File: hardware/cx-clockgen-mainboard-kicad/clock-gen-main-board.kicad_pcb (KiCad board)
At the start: 2 copper layers, 70 x 64.4 mm, 17 parts, among them J1 Conn_01x03_Pin, J2 Conn_01x03_Pin, J3 Headswitch_SMA, J8 Conn_Coaxial, U1 Pico

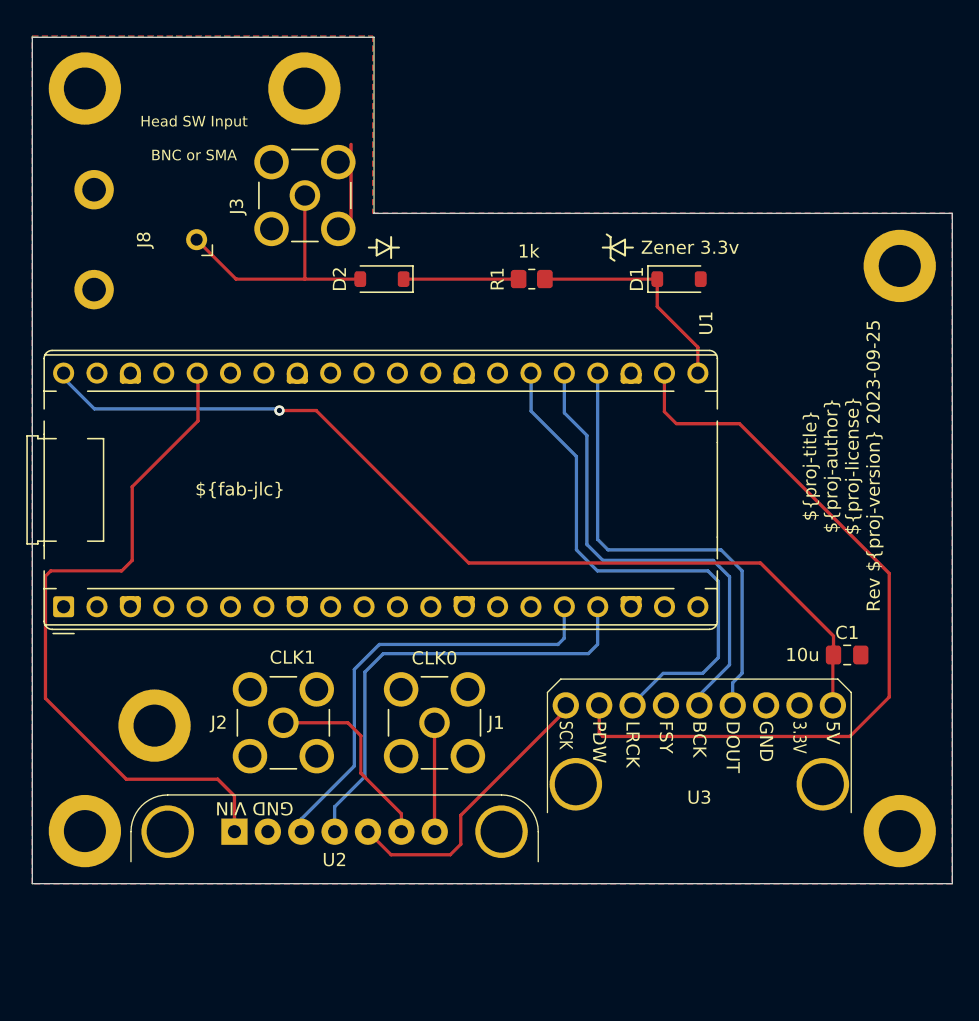
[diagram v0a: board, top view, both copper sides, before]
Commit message: Update KiCad project files: modified project title and version, adjusted component properties, and streamlined pin functions for clarity. Removed obsolete library references and updated netlist handling for improved error management. Enhanced design parameters and added new connector symbols for better integration.
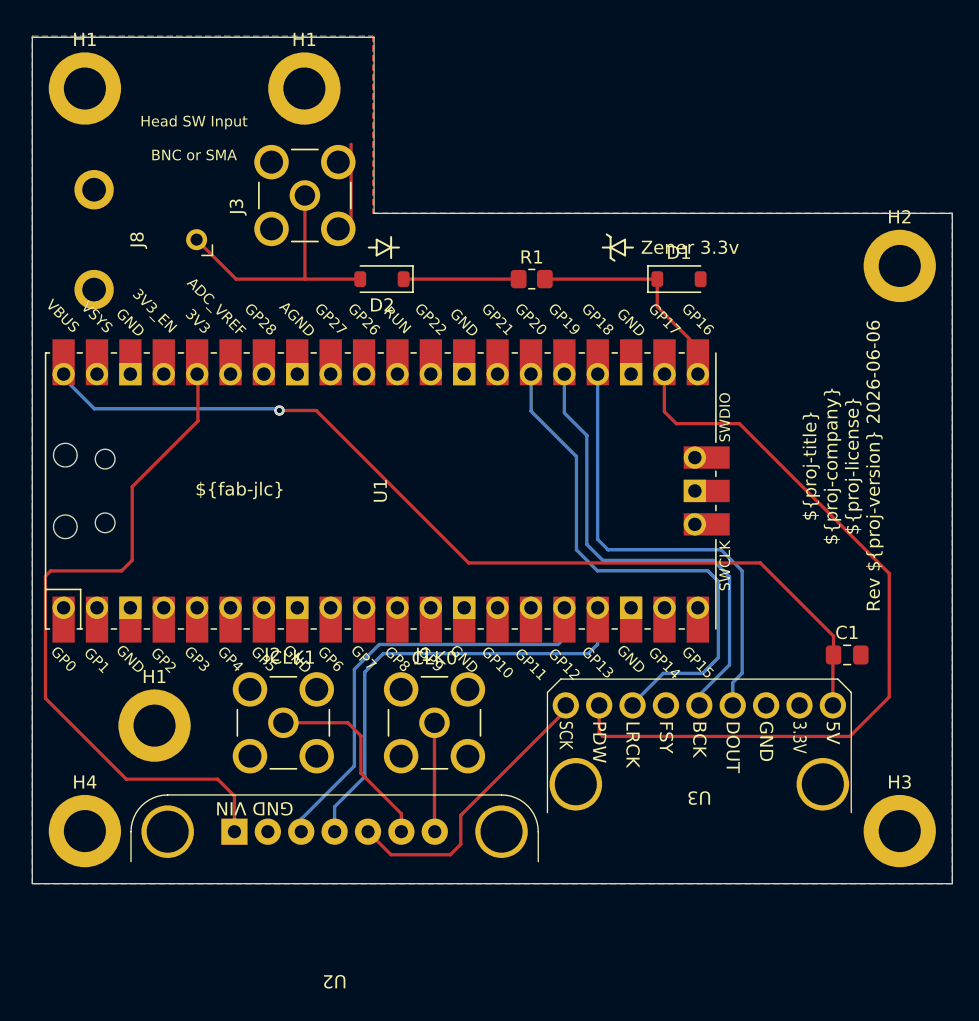
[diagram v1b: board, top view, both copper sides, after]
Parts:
- U1: footprint Module:RaspberryPi_Pico_Common_THT -> GDH Modules:Pi_Pico_SMD_TH
- moved U1 25.7 mm to (124.5, 100.1)
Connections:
- U2 pad 0: Net-(U2-CLK0) -> (no net)
